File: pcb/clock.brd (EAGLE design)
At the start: 107.8 x 42.2 mm, 50 parts, among them K1 JS-M1-9V-4, K2 JS-M1-9V-4, Q1 BC447, Q2 BC447, Q3 BC447, Q4 BC447, Q5 BC447, Q6 BC447, Q8 CSM-7X-DU, Q9 MC-306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

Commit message: some small things
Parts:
- added C2: (no value), rcl:C1206
- added C7: (no value), rcl:C025-040X050
- added D1: (no value), diode:SOD80C
- added R23: (no value), rcl:R1206
- moved JP1 20.6 mm to (51.8, 59.7), flipped to the bottom, turned to 90 degrees
- moved R6 16.8 mm to (54.5, 21.7), turned to 90 degrees
- moved U$5 9.72 mm to (94.9, 58.5)
- moved U$4 9.11 mm to (80.2, 58.5)
- moved U$3 8.19 mm to (65.3, 58.5)
- moved D2 5.96 mm to (96.3, 18.2)
- moved U$1 5.31 mm to (3.81, 57.5)
- moved R5 3.50 mm to (47.9, 24.6)
- moved C1 2.69 mm to (92.9, 30.1)
- moved R21 2.10 mm to (51.0, 22.5), turned to 90 degrees
- moved R8 1.19 mm to (58.0, 38.3)
- moved IC1 1.04 mm to (91.8, 24.2)
- moved X1 0.95 mm to (95.4, 36.8)
- moved R22 0.48 mm to (47.9, 18.9)
- moved U1 0.32 mm to (57.9, 29.7)
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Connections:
- removed net AVCC: U1.18
- new net N$66: C2.2, U1.20
- new net N$67: D1.C, D2.C, R23.2
- new net N$68: R23.1, U2.8
- net GND: now also C2.1, C7.2
- net VCC: now also C7.1, D1.A, U1.18; no longer D2.C, U2.8
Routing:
- net VCC: track 325.8 -> 225.8 mm
- net N$67: track 0.00 -> 73.7 mm
- net N$52: track 0.00 -> 73.2 mm
- net N$51: track 0.00 -> 67.3 mm, vias 0 -> 1
- net N$54: track 0.00 -> 55.3 mm, vias 0 -> 1
- net N$55: track 0.00 -> 53.6 mm, vias 0 -> 2
- net N$49: track 0.00 -> 53.3 mm, vias 0 -> 1
- net N$53: track 7.21 -> 51.3 mm, vias 0 -> 2
- net N$32: track 0.00 -> 40.5 mm
- net N$50: track 0.00 -> 37.1 mm, vias 0 -> 1
- net N$58: track 0.00 -> 36.4 mm
- net N$44: track 0.00 -> 29.0 mm
- net N$59: track 0.00 -> 27.5 mm
- net N$60: track 0.00 -> 24.0 mm
- net N$56: track 4.64 -> 26.8 mm
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- added copper zone on layer 1, net GND
- added copper zone on layer 16, net GND
- added copper zone on layer 16, net VCC
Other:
- board size 107.8 x 42.2 mm -> 109.7 x 74.2 mm

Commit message: add adc
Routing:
- net VCC: track 225.8 -> 188.8 mm
- net GND: track 260.0 -> 246.5 mm
- net N$51: track 67.3 -> 64.9 mm
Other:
- board size 109.7 x 74.2 mm -> 109.7 x 74.5 mm

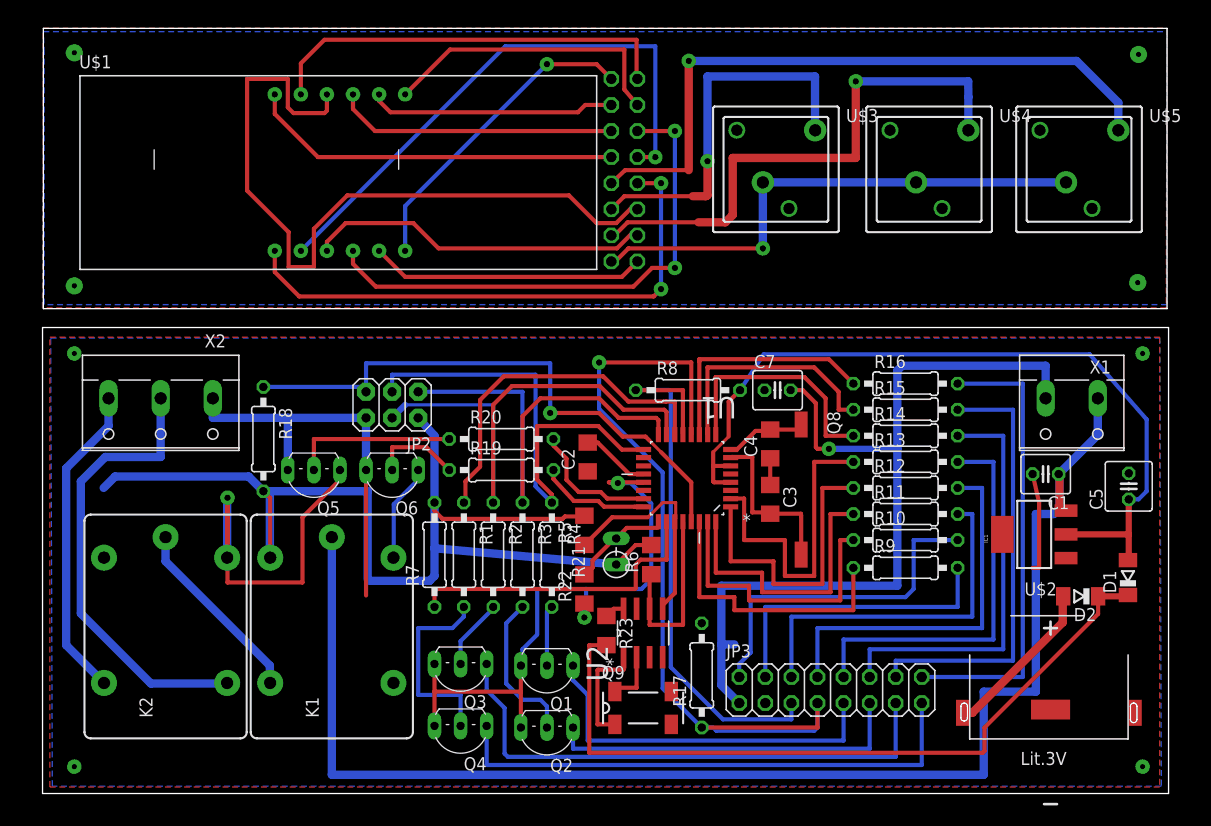
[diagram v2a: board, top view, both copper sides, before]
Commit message: finishing pcb
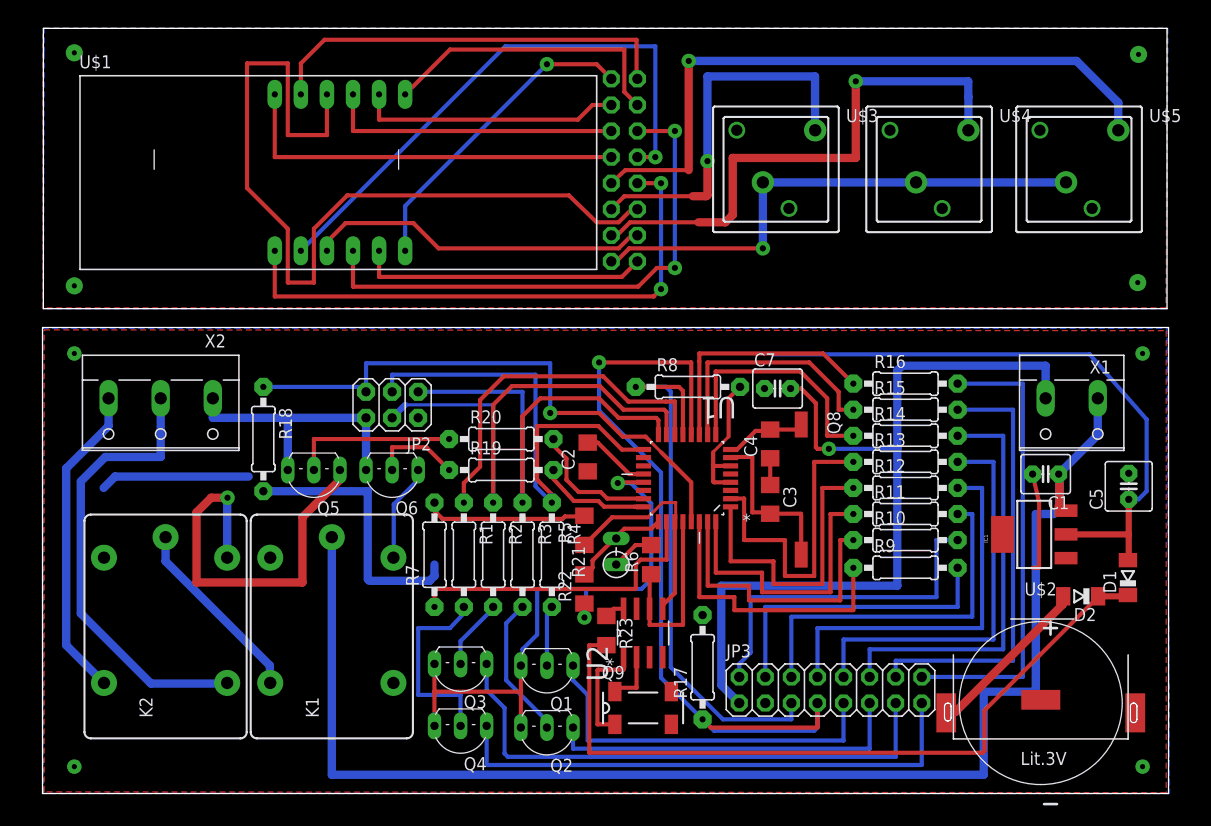
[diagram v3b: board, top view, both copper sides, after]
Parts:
- moved R17 0.80 mm to (59.5, 11.3)
- moved R8 0.32 mm to (58.0, 38.6)
- moved C7 0.16 mm to (66.8, 38.4)
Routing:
- net VCC: track 188.8 -> 136.1 mm
- net GND: track 246.5 -> 231.2 mm
- net N$52: track 73.2 -> 84.0 mm
- net N$58: track 36.4 -> 38.9 mm
- net N$60: track 24.0 -> 25.7 mm
- net N$56: track 26.8 -> 28.3 mm
- net N$55: track 53.6 -> 55.0 mm
- net N$53: track 51.3 -> 52.6 mm
- net N$59: track 27.5 -> 28.7 mm
- net N$5: track 15.1 -> 14.0 mm
- net N$14: track 23.3 -> 24.1 mm
- net N$11: track 23.5 -> 24.3 mm
- net N$40: track 38.4 -> 39.1 mm
- net N$13: track 23.5 -> 24.2 mm
- net N$43: track 16.0 -> 16.5 mm

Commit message: some changes problem with set time
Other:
- board size 109.7 x 74.5 mm -> 110.3 x 75.2 mm

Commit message: extend board
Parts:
- removed C4: (no value), rcl:C1206
- added C6: (no value), rcl:C0805K
- C3: device rcl:C1206 -> rcl:C0805K
- moved C3 5.72 mm to (65.1, 33.3), turned to 90 degrees
- moved R5 2.46 mm to (45.6, 24.0)
- moved R22 2.38 mm to (45.6, 18.8)
- moved R4 1.83 mm to (42.9, 22.3)
- moved R19 1.81 mm to (38.1, 31.0)
- moved R20 1.75 mm to (38.1, 33.6)
- moved R3 1.67 mm to (40.2, 22.3)
- moved R21 1.64 mm to (49.5, 21.9)
- moved Q2 1.59 mm to (42.7, 4.21)
- moved Q1 1.53 mm to (42.8, 10.4)
- moved Q3 1.43 mm to (34.4, 10.4)
- moved R2 1.43 mm to (37.6, 22.3)
- moved Q4 1.43 mm to (34.4, 4.29)
- moved C1 1.35 mm to (94.2, 30.1)
- moved R17 1.32 mm to (58.3, 10.6)
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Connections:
- net GND: now also C6.1; no longer C4.1
- net N$30: now also C6.2; no longer C3.2
- net N$31: now also C3.2; no longer C4.2
- net N$35: now also JP3.3
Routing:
- net VCC: track 136.1 -> 199.5 mm
- net N$35: track 30.6 -> 75.2 mm
- net N$67: track 73.7 -> 58.7 mm
- net N$45: track 44.4 -> 32.4 mm
- net N$52: track 84.0 -> 73.2 mm
- net GND: track 231.2 -> 240.6 mm
- net N$28: track 19.3 -> 24.7 mm
- net N$12: track 136.1 -> 139.7 mm
- net RESET: track 56.4 -> 53.6 mm
- net N$2: track 21.4 -> 24.2 mm
- net N$34: track 10.8 -> 13.4 mm
- net N$58: track 38.9 -> 36.4 mm
- net N$33: track 12.7 -> 15.1 mm
- net N$36: track 9.75 -> 12.1 mm
- net N$30: track 16.4 -> 14.1 mm
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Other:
- board size 110.3 x 75.2 mm -> 110.3 x 74 mm

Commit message: temp stable version
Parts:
- removed D1: (no value), diode:SOD80C
- removed R23: (no value), rcl:R1206
- added D3: ES2D, diode:SMB
- moved D2 1.59 mm to (94.7, 18.2)
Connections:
- removed net N$68: R23.1, U2.8
- net N$67: now also D3.C, U2.8; no longer D1.C, R23.2
- net VCC: now also D3.A; no longer D1.A
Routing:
- net N$67: track 58.7 -> 56.3 mm
- net N$68: track 1.90 -> 0.00 mm
- net N$43: track 16.0 -> 14.8 mm
- net VCC: track 199.5 -> 198.5 mm
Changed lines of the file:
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@@
 </element>
 <element name="U$2" library="battery" package="CR3232" value="CR1632" x="93.345" y="8.09625"/>
-<element name="D2" library="diode" package="SOD80C" value="" x="96.281875" y="18.176875" rot="R180"/>
+<element name="D2" library="diode" package="SOD80C" value="" x="94.694375" y="18.176875" rot="R180"/>
 <element name="Q9" library="quarz" package="MC-306" value="MC-306" x="52.625625" y="7.381875">
 <attribute name="OC_NEWARK" value="31M5576" x="52.625625" y="7.381875" size="1.778" layer="27" display="off"/>
@@
 <element name="C2" library="rcl" package="C1206" value="" x="47.863125" y="30.95625" rot="R90"/>
 <element name="C7" library="rcl" package="C025-040X050" value="" x="66.83375" y="38.25875"/>
-<element name="D1" library="diode" package="SOD80C" value="" x="100.885625" y="20.0025" rot="R90"/>
-<element name="R23" library="rcl" package="R1206" value="" x="49.05375" y="14.9225" rot="R270"/>
 <element name="C6" library="rcl" package="C0805K" value="" x="65.166875" y="27.860625" rot="R270"/>
 <element name="C3" library="rcl" package="C0805K" value="" x="65.0875" y="33.258125" rot="R90"/>
+<element name="D3" library="diode" package="SMB" value="ES2D" x="100.885625" y="20.47875" rot="R90"/>
 </elements>
 <signals>
@@
 <wire x1="59.451875" y1="29.448125" x2="59.451875" y2="30.95625" width="0.4064" layer="1"/>
 <contactref element="C5" pad="1"/>
-<wire x1="94.8563" y1="24.209375" x2="100.965" y2="24.209375" width="0.6096" layer="1"/>
 <wire x1="100.965" y1="27.6225" x2="101.9175" y2="27.6225" width="0.4064" layer="16"/>
 <wire x1="64.373125" y1="41.830625" x2="62.468125" y2="38.496875" width="0.4064" layer="16"/>
-<wire x1="100.965" y1="27.6225" x2="100.965" y2="24.209375" width="0.6096" layer="1"/>
 <wire x1="15.636875" y1="28.495625" x2="16.304375" y2="27.828125" width="0.4064" layer="1"/>
 <wire x1="16.304375" y1="27.828125" x2="16.304375" y2="22.019375" width="0.4064" layer="1"/>
@@
 <contactref element="U1" pad="18"/>
 <contactref element="C7" pad="1"/>
-<contactref element="D1" pad="A"/>
-<wire x1="100.965" y1="24.209375" x2="100.965" y2="21.781875" width="0.6096" layer="1"/>
-<wire x1="100.965" y1="21.781875" x2="100.885625" y2="21.7025" width="0.6096" layer="1"/>
 <wire x1="52.69825" y1="23.17075" x2="53.419375" y2="23.250125" width="0.4064" layer="1"/>
 <wire x1="49.53" y1="20.6375" x2="49.05375" y2="21.351875" width="0.6096" layer="16"/>
@@
 <wire x1="53.34675" y1="23.1775" x2="53.419375" y2="23.250125" width="0.4064" layer="1"/>
 <wire x1="45.157625" y1="25.796875" x2="45.56125" y2="25.39325" width="0.4064" layer="1"/>
+<contactref element="D3" pad="A"/>
+<wire x1="100.965" y1="27.6225" x2="100.965" y2="24.28875" width="0.6096" layer="1"/>
+<wire x1="100.965" y1="24.28875" x2="100.965" y2="22.758125" width="0.6096" layer="1"/>
+<wire x1="100.965" y1="22.758125" x2="100.885625" y2="22.67875" width="0.6096" layer="1"/>
+<wire x1="94.8563" y1="24.209375" x2="100.885625" y2="24.209375" width="0.6096" layer="1"/>
+<wire x1="100.885625" y1="24.209375" x2="100.965" y2="24.28875" width="0.6096" layer="1"/>
 <wire x1="59.451875" y1="32.305625" x2="52.670075" y2="31.772225" width="0" layer="19" extent="1-1"/>
 </signal>
@@
 <wire x1="61.991875" y1="7.858125" x2="62.5475" y2="7.858125" width="0.8128" layer="16"/>
 <wire x1="31.90875" y1="11.668125" x2="31.90875" y2="11.58875" width="0" layer="19" extent="16-16"/>
+<wire x1="60.245625" y1="9.604375" x2="54.530625" y2="12.2428" width="0" layer="19" extent="1-16"/>
 <wire x1="78.26375" y1="32.7025" x2="78.105" y2="40.16375" width="0" layer="19" extent="16-16"/>
 <wire x1="65.325625" y1="52.07" x2="68.024375" y2="38.25875" width="0" layer="19" extent="1-16"/>
@@
 <contactref element="U$2" pad="VCC"/>
 <contactref element="D2" pad="A"/>
-<wire x1="94.581875" y1="18.176875" x2="94.535625" y2="18.130625" width="0.8128" layer="1"/>
-<wire x1="94.535625" y1="18.130625" x2="94.535625" y2="15.636875" width="0.8128" layer="1"/>
-<wire x1="94.535625" y1="15.636875" x2="85.725" y2="6.82625" width="0.8128" layer="1"/>
-<wire x1="85.725" y1="6.82625" x2="84.7725" y2="6.82625" width="0.8128" layer="1"/>
+<wire x1="92.994375" y1="18.176875" x2="92.994375" y2="15.048125" width="0.8128" layer="1"/>
+<wire x1="92.994375" y1="15.048125" x2="84.7725" y2="6.82625" width="0.8128" layer="1"/>
 </signal>
 <signal name="N$32">
@@
 <signal name="N$67">
 <contactref element="D2" pad="C"/>
-<contactref element="D1" pad="C"/>
-<wire x1="97.981875" y1="18.176875" x2="100.76" y2="18.176875" width="0.6096" layer="1"/>
-<wire x1="100.76" y1="18.176875" x2="100.885625" y2="18.3025" width="0.6096" layer="1"/>
-<wire x1="97.981875" y1="18.176875" x2="97.869375" y2="18.064375" width="0.4064" layer="1"/>
-<wire x1="88.42375" y1="14.2875" x2="49.05375" y2="14.2875" width="0.4064" layer="1"/>
-<wire x1="49.05375" y1="14.2875" x2="49.047" y2="13.49375" width="0.4064" layer="1"/>
-<contactref element="R23" pad="2"/>
-<wire x1="49.047" y1="13.49375" x2="49.2125" y2="13.49375" width="0.4064" layer="1"/>
-<wire x1="49.05375" y1="13.5005" x2="49.047" y2="13.49375" width="0.4064" layer="1"/>
-<wire x1="88.42375" y1="14.2875" x2="88.42375" y2="16.8275" width="0.4064" layer="1"/>
-<wire x1="88.42375" y1="16.8275" x2="91.59875" y2="20.0025" width="0.4064" layer="1"/>
-<wire x1="91.59875" y1="20.0025" x2="97.94875" y2="20.0025" width="0.4064" layer="1"/>
-<wire x1="97.94875" y1="20.0025" x2="97.94875" y2="18.21" width="0.4064" layer="1"/>
-<wire x1="97.94875" y1="18.21" x2="97.981875" y2="18.176875" width="0.4064" layer="1"/>
-</signal>
-<signal name="N$68">
+<wire x1="96.36125" y1="18.21" x2="96.394375" y2="18.176875" width="0.4064" layer="1"/>
+<contactref element="D3" pad="C"/>
+<wire x1="96.394375" y1="18.176875" x2="100.78375" y2="18.176875" width="0.8128" layer="1"/>
+<wire x1="100.78375" y1="18.176875" x2="100.885625" y2="18.27875" width="0.8128" layer="1"/>
 <contactref element="U2" pad="8"/>
-<contactref element="R23" pad="1"/>
-<wire x1="49.05375" y1="16.3445" x2="49.755825" y2="16.9672" width="0.4064" layer="1"/>
-<wire x1="49.755825" y1="16.9672" x2="50.720625" y2="16.9672" width="0.4064" layer="1"/>
+<wire x1="96.36125" y1="18.21" x2="96.36125" y2="18.811875" width="0.6096" layer="1"/>
+<wire x1="96.36125" y1="18.811875" x2="95.170625" y2="20.0025" width="0.6096" layer="1"/>
+<wire x1="95.170625" y1="20.0025" x2="90.64625" y2="20.0025" width="0.6096" layer="1"/>
+<wire x1="90.64625" y1="20.0025" x2="84.93125" y2="14.2875" width="0.6096" layer="1"/>
+<wire x1="84.93125" y1="14.2875" x2="50.879375" y2="14.2875" width="0.6096" layer="1"/>
+<wire x1="50.879375" y1="14.2875" x2="50.8" y2="14.366875" width="0.6096" layer="1"/>
+<wire x1="50.8" y1="14.366875" x2="50.8" y2="16.887825" width="0.6096" layer="1"/>
+<wire x1="50.8" y1="16.887825" x2="50.720625" y2="16.9672" width="0.6096" layer="1"/>
 </signal>
 <signal name="N$69">

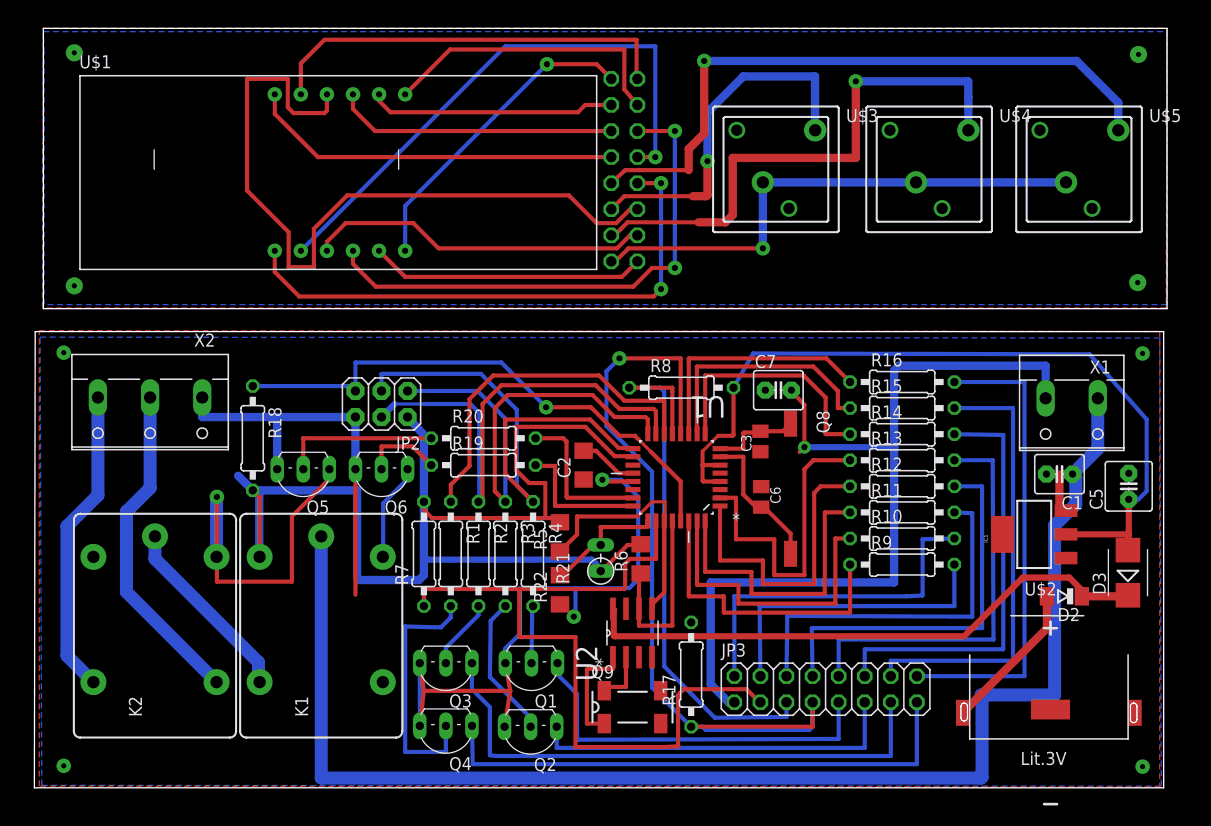
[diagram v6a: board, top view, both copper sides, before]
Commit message: board modification for use external device, move thermistor to adc6, software is not modificated yet
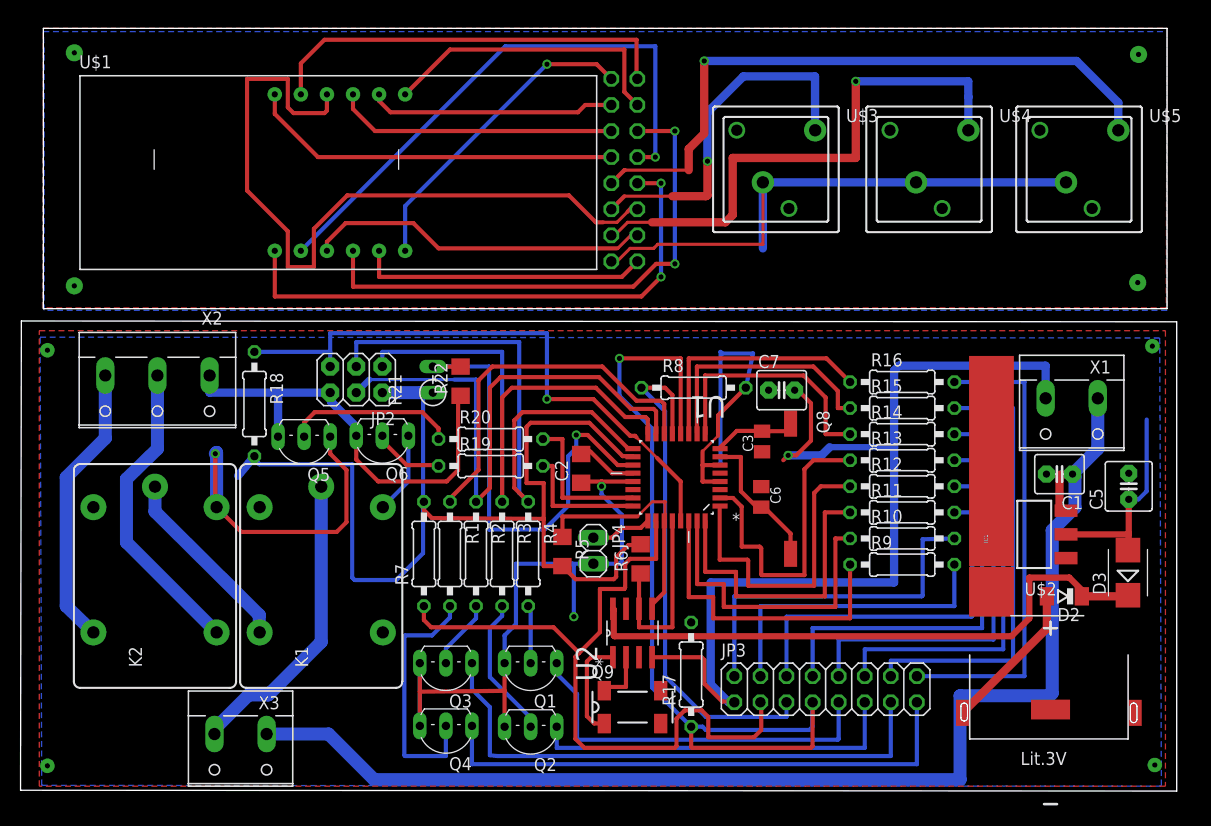
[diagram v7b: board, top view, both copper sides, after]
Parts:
- added JP4: (no value), pinhead:1X02
- added X3: (no value), con-wago-508:W237-132
- moved R21 23.9 mm to (33.2, 39.3)
- moved R22 22.5 mm to (35.9, 39.1)
- moved K1 4.84 mm to (22.3, 20.2)
- moved K2 4.84 mm to (6.11, 20.2)
- moved JP2 3.42 mm to (25.7, 39.3)
- moved R18 3.34 mm to (15.8, 36.9)
- moved Q6 3.26 mm to (28.3, 32.5)
- moved Q5 3.18 mm to (20.6, 32.5)
- moved X2 2.26 mm to (6.35, 39.1)
- moved R5 1.45 mm to (45.8, 22.5), turned to 270 degrees
- moved R8 1.19 mm to (58.6, 38.5)
- moved R19 0.72 mm to (38.8, 30.9)
- moved R20 0.72 mm to (38.8, 33.5)
- moved R4 0.48 mm to (42.5, 22.3)
- moved C2 0.40 mm to (47.6, 30.6)
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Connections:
- new net N$68: JP4.1, U1.25
- new net N$73: C1.1, IC1.3, X1.1, X3.1
- net GND: now also JP4.2
- net N$12: now also X3.2; no longer C1.1, IC1.3, X1.1
- net N$36: now also U1.19; no longer U1.25
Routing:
- net N$73: track 0.00 -> 123.1 mm
- net N$12: track 139.7 -> 29.5 mm
- net VCC: track 198.5 -> 156.9 mm
- net N$36: track 12.1 -> 46.7 mm, vias 0 -> 1
- net GND: track 240.6 -> 268.7 mm, vias 4 -> 3
- net MISO: track 46.1 -> 55.1 mm
- net SCK: track 49.0 -> 56.0 mm
- net MOSI: track 49.7 -> 56.0 mm
- net N$68: track 0.00 -> 5.98 mm
- net RESET: track 53.6 -> 58.4 mm
- net N$40: track 38.4 -> 33.8 mm
- net N$37: track 54.5 -> 51.0 mm
- net N$35: track 75.2 -> 72.0 mm
- net N$15: track 81.8 -> 84.7 mm
- net N$45: track 32.4 -> 29.9 mm
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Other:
- board size 110.3 x 74 mm -> 112.6 x 74.3 mm
